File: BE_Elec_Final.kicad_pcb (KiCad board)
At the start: 2 copper layers, 110 x 100 mm, 54 parts, among them J2 Conn_01x02, J3 Conn_01x03, Q1 2N2907, Q10 TIP32, Q11 BD138, Q12 TIP31, Q13 2N222, Q2 2N2907, Q3 2N2907, Q4 2N222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

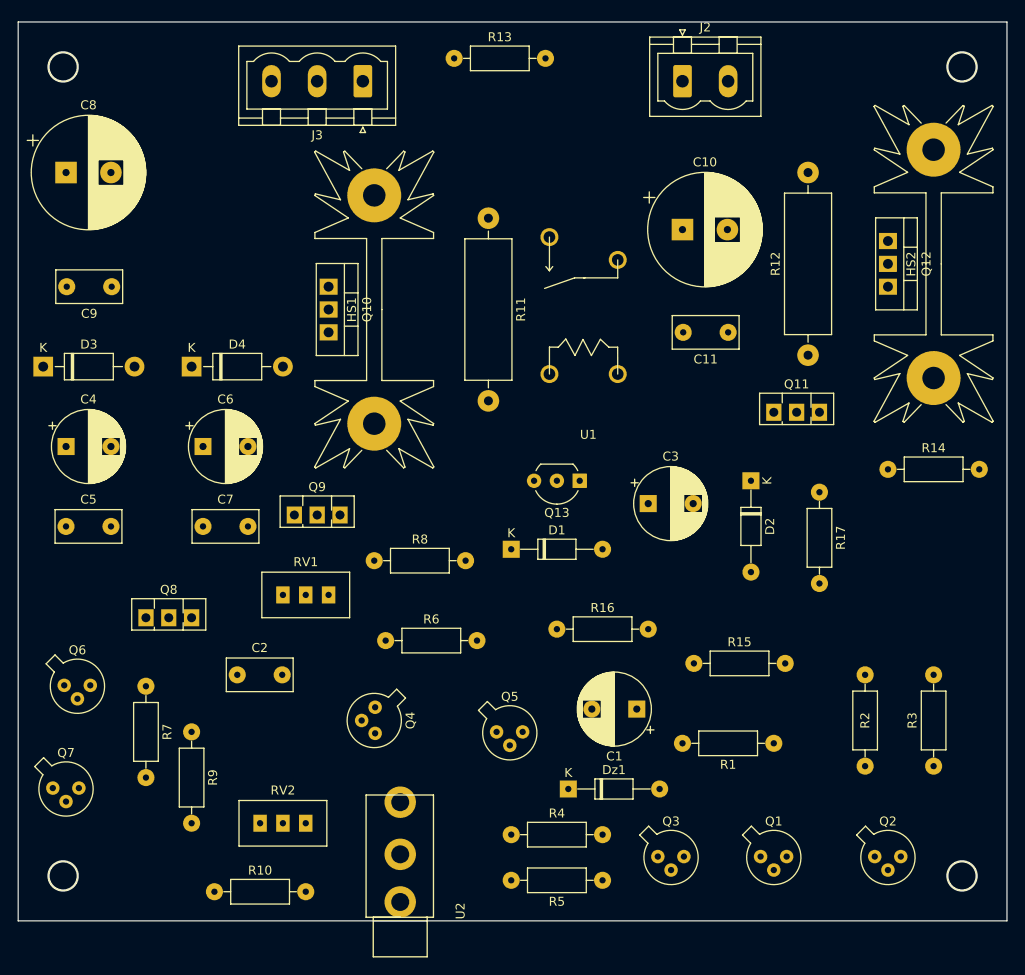
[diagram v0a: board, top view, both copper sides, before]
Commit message: Mise à jour netlist et dernières modifications de placement.
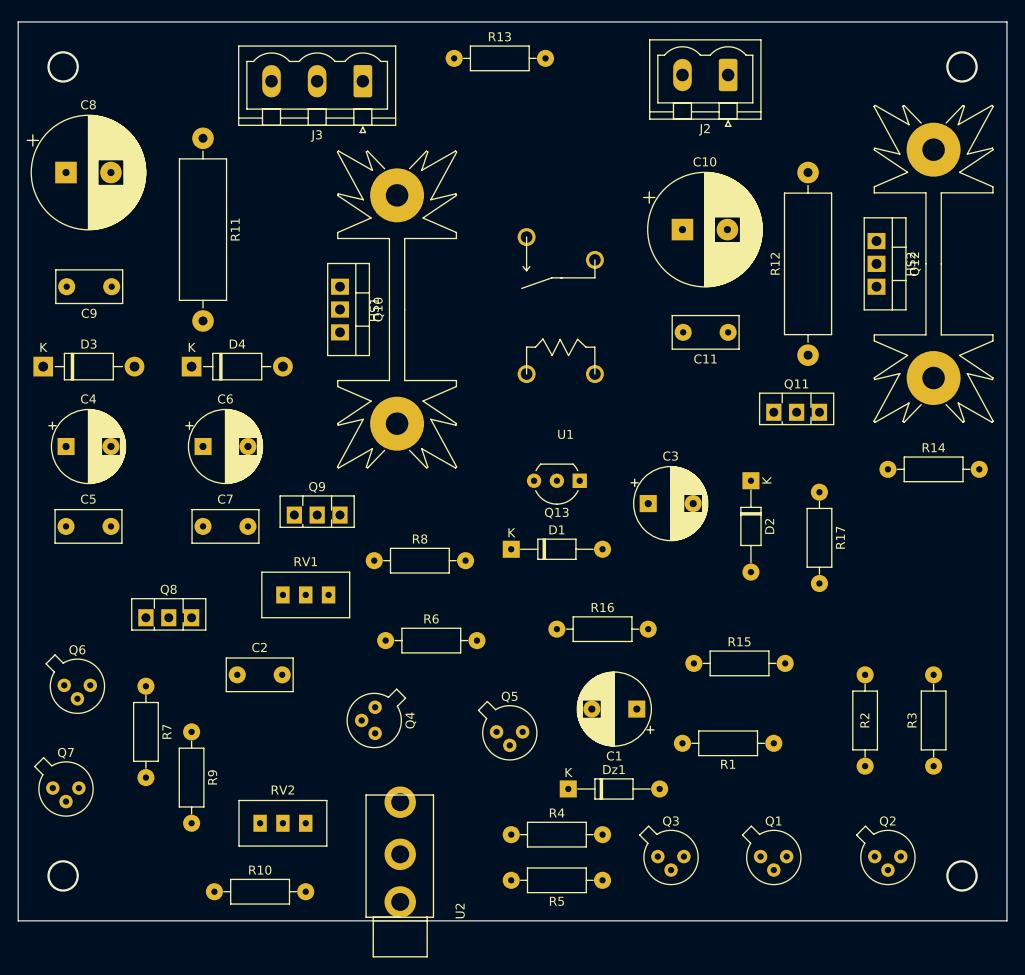
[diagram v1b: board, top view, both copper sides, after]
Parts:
- moved R11 33.0 mm to (35.6, 27.9)
- moved J2 5.13 mm to (94.0, 20.9), turned to 180 degrees
- moved U1 2.54 mm to (69.8, 55.9)
- moved HS1 2.54 mm to (57.1, 47.0)
- moved Q12 1.27 mm to (110.5, 39.4)
- moved Q10 1.27 mm to (50.8, 44.5)
